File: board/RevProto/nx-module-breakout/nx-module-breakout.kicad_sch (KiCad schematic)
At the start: 8 parts, among them J1 Conn_02x15_Odd_Even, J2 DF40C-60DS-0.4V(51), J3 Conn_02x15_Odd_Even, J4 Conn_02x15_Odd_Even, J5 DF40C-60DS-0.4V(51), J6 SFV22R-2STE1HLF, J7 SFV22R-2STE1HLF, J8 Conn_02x06_Odd_Even

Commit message: nx module breakout work in progress
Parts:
- J6, J7: footprint RP2350_60QFN_minimal:AMPHENOL_SFV22R-2STE1HLF -> CUSTOM:AMPHENOL_SFV22R-2STE1HLF
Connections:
- net DPHY0_CLK+: now also J7.9 (Pin_9); no longer J6.9 (Pin_9)
- net DPHY0_CLK-: now also J7.8 (Pin_8); no longer J6.8 (Pin_8)
- net DPHY0_D0+: now also J7.3 (Pin_3); no longer J6.3 (Pin_3)
- net DPHY0_D0-: now also J7.2 (Pin_2); no longer J6.2 (Pin_2)
- net DPHY0_D1+: now also J7.6 (Pin_6); no longer J6.6 (Pin_6)
- net DPHY0_D1-: now also J7.5 (Pin_5); no longer J6.5 (Pin_5)
- net DPHY0_D2+: now also J7.12 (Pin_12); no longer J6.12 (Pin_12)
- net DPHY0_D2-: now also J7.11 (Pin_11); no longer J6.11 (Pin_11)
- net DPHY0_D3+: now also J7.15 (Pin_15); no longer J6.15 (Pin_15)
- net DPHY0_D3-: now also J7.14 (Pin_14); no longer J6.14 (Pin_14)
- net DPHY1_CLK+: now also J6.14 (Pin_14); no longer J7.14 (Pin_14)
- net DPHY1_CLK-: now also J6.15 (Pin_15); no longer J7.15 (Pin_15)
- net DPHY1_D0+: now also J6.20 (Pin_20); no longer J7.20 (Pin_20)
- net DPHY1_D0-: now also J6.21 (Pin_21); no longer J7.21 (Pin_21)
- net DPHY1_D1+: now also J6.17 (Pin_17); no longer J7.17 (Pin_17)
- net DPHY1_D1-: now also J6.18 (Pin_18); no longer J7.18 (Pin_18)
- net DPHY1_D2+: now also J6.11 (Pin_11); no longer J7.11 (Pin_11)
- net DPHY1_D2-: now also J6.12 (Pin_12); no longer J7.12 (Pin_12)
- net DPHY1_D3+: now also J6.8 (Pin_8); no longer J7.8 (Pin_8)
- net DPHY1_D3-: now also J6.9 (Pin_9); no longer J7.9 (Pin_9)
- net GND: now also J1.1 (Pin_1), J1.11 (Pin_11), J1.12 (Pin_12), J1.2 (Pin_2), J1.21 (Pin_21), J1.22 (Pin_22), J6.22 (Pin_22), J7.1 (Pin_1); no longer J1.10 (Pin_10), J1.19 (Pin_19), J1.20 (Pin_20), J1.29 (Pin_29), J1.30 (Pin_30), J1.9 (Pin_9), J6.1 (Pin_1), J6.MP (MountPin), J7.22 (Pin_22), J7.MP (MountPin)
- net LED_EN0: now also J6.5 (Pin_5); no longer J6.18 (Pin_18)
- net LED_EN1: now also J7.18 (Pin_18); no longer J7.5 (Pin_5)
- net P3V3D: now also J6.1 (Pin_1), J7.22 (Pin_22); no longer J6.22 (Pin_22), J7.1 (Pin_1)
- net PB56N: now also J1.14 (Pin_14); no longer J1.11 (Pin_11)
- net PB56P: now also J1.13 (Pin_13); no longer J1.12 (Pin_12)
- net PB58N: now also J1.7 (Pin_7); no longer J1.6 (Pin_6)
- net PB58P: now also J1.8 (Pin_8); no longer J1.5 (Pin_5)
- net PB60N: now also J1.9 (Pin_9); no longer J1.8 (Pin_8)
- net PB60P: now also J1.10 (Pin_10); no longer J1.7 (Pin_7)
- net PB62N: now also J1.16 (Pin_16); no longer J1.13 (Pin_13)
- net PB62P: now also J1.15 (Pin_15); no longer J1.14 (Pin_14)
- net PB64N: now also J1.17 (Pin_17); no longer J1.16 (Pin_16)
- net PB64P: now also J1.18 (Pin_18); no longer J1.15 (Pin_15)
- net PB66N: now also J1.19 (Pin_19); no longer J1.18 (Pin_18)
- net PB66P: now also J1.20 (Pin_20); no longer J1.17 (Pin_17)
- net PB68N: now also J1.23 (Pin_23); no longer J1.22 (Pin_22)
- net PB68P: now also J1.24 (Pin_24); no longer J1.21 (Pin_21)
- net PB70N: now also J1.26 (Pin_26); no longer J1.23 (Pin_23)
- net PB70P: now also J1.25 (Pin_25); no longer J1.24 (Pin_24)
- net PR11N: now also J1.29 (Pin_29); no longer J1.28 (Pin_28)
- net PR11P: now also J1.30 (Pin_30); no longer J1.27 (Pin_27)
- net PR13N: now also J1.27 (Pin_27); no longer J1.26 (Pin_26)
- net PR13P: now also J1.28 (Pin_28); no longer J1.25 (Pin_25)
- net PR7N: now also J4.27 (Pin_27); no longer J1.3 (Pin_3)
- net PR7P: now also J4.28 (Pin_28); no longer J1.4 (Pin_4)
- net PT67N: now also J4.25 (Pin_25); no longer J1.1 (Pin_1)
- net PT67P: now also J4.26 (Pin_26); no longer J1.2 (Pin_2)
- net PWR_EN0: now also J6.6 (Pin_6); no longer J6.17 (Pin_17)
- net PWR_EN1: now also J7.17 (Pin_17); no longer J7.6 (Pin_6)
- net SCL0: now also J6.3 (Pin_3); no longer J6.20 (Pin_20)
- net SCL1: now also J7.20 (Pin_20); no longer J7.3 (Pin_3)
- net SDA0: now also J6.2 (Pin_2); no longer J6.21 (Pin_21)
- net SDA1: now also J7.21 (Pin_21); no longer J7.2 (Pin_2)
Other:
- moved on the sheet: J1, J2, J3, J4, J5, J6, J7, J8

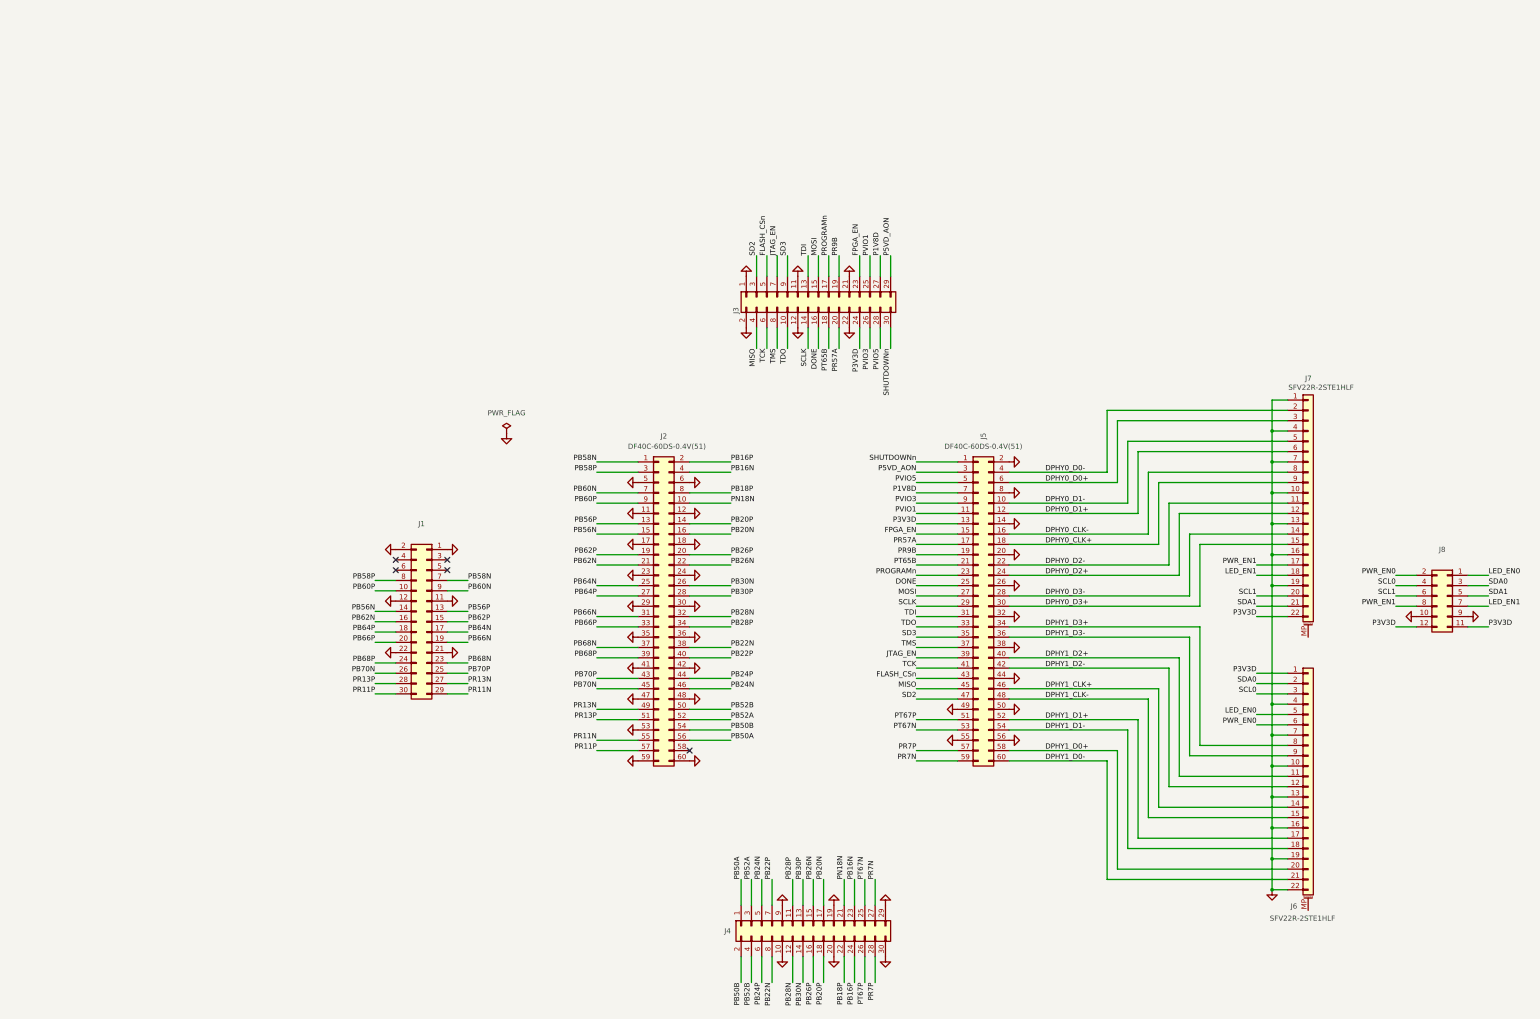
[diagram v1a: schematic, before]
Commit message: Consistent schematic & PCB connector orientation for module, breakout board and pico2-nx.
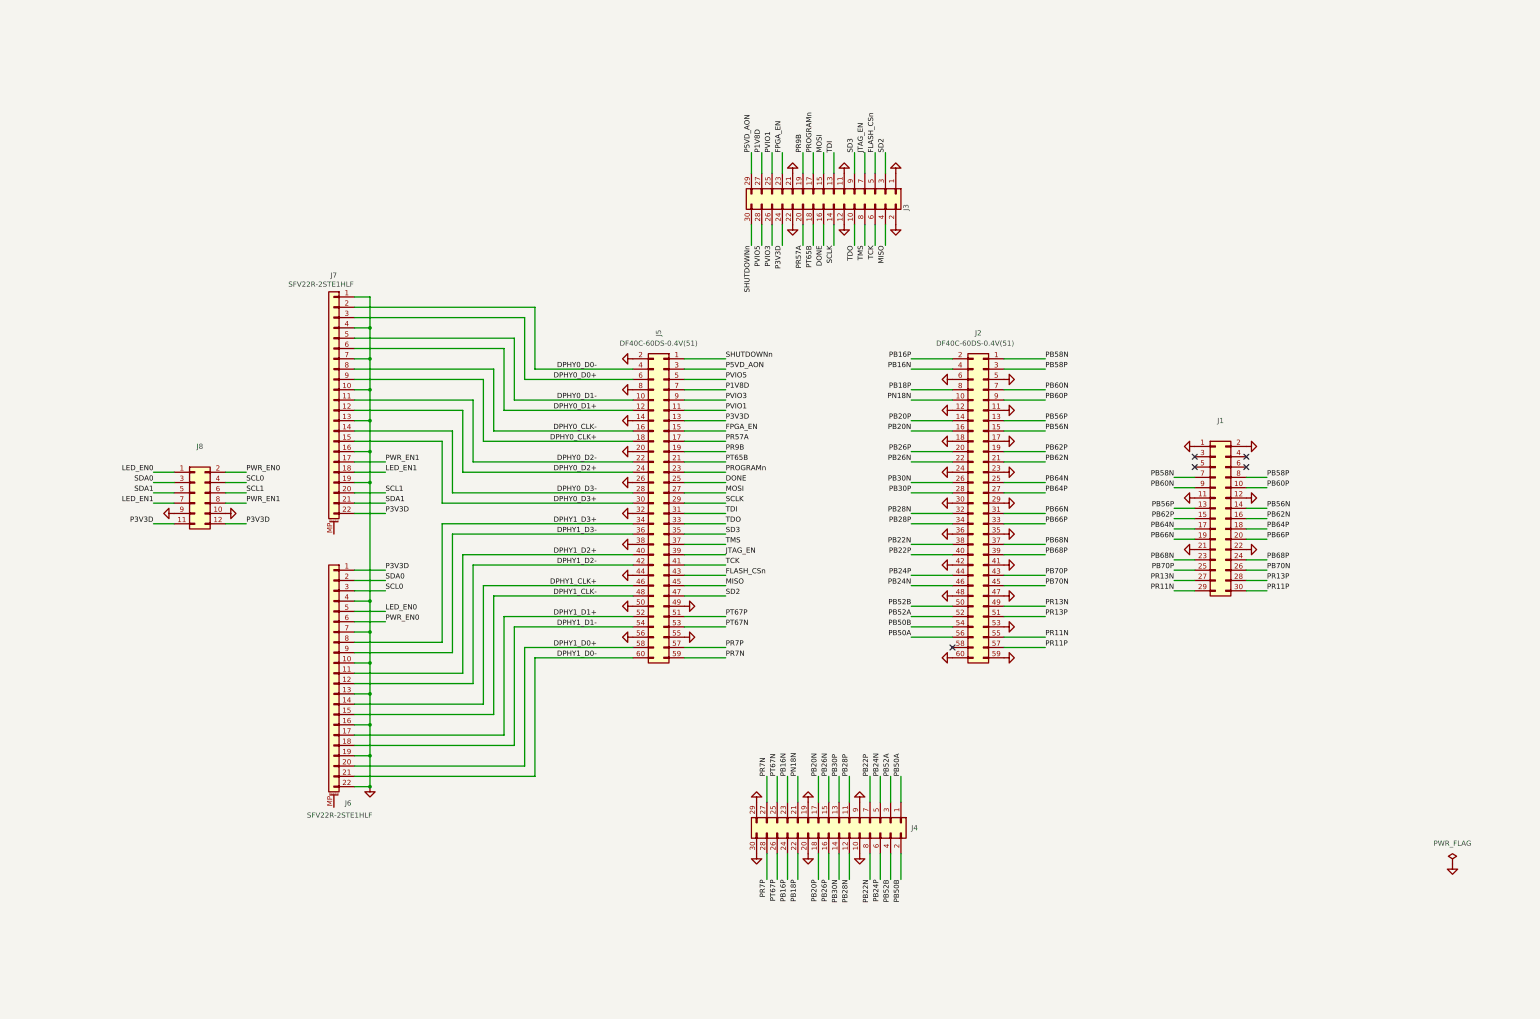
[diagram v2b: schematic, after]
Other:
- moved on the sheet: J1, J2, J3, J4, J5, J6, J7, J8

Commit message: Route breakout
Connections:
- net GND: now also J6.MP (MountPin), J7.MP (MountPin)
- net LED_EN0: now also J8.6 (Pin_6); no longer J8.1 (Pin_1)
- net LED_EN1: now also J8.5 (Pin_5); no longer J8.7 (Pin_7)
- net PB56N: now also J1.13 (Pin_13); no longer J1.14 (Pin_14)
- net PB56P: now also J1.14 (Pin_14); no longer J1.13 (Pin_13)
- net PB58N: now also J1.8 (Pin_8); no longer J1.7 (Pin_7)
- net PB58P: now also J1.7 (Pin_7); no longer J1.8 (Pin_8)
- net PB60N: now also J1.10 (Pin_10); no longer J1.9 (Pin_9)
- net PB60P: now also J1.9 (Pin_9); no longer J1.10 (Pin_10)
- net PB62N: now also J1.15 (Pin_15); no longer J1.16 (Pin_16)
- net PB62P: now also J1.16 (Pin_16); no longer J1.15 (Pin_15)
- net PB64N: now also J1.18 (Pin_18); no longer J1.17 (Pin_17)
- net PB64P: now also J1.17 (Pin_17); no longer J1.18 (Pin_18)
- net PB66N: now also J1.20 (Pin_20); no longer J1.19 (Pin_19)
- net PB66P: now also J1.19 (Pin_19); no longer J1.20 (Pin_20)
- net PB68N: now also J1.24 (Pin_24); no longer J1.23 (Pin_23)
- net PB68P: now also J1.23 (Pin_23); no longer J1.24 (Pin_24)
- net PB70N: now also J1.25 (Pin_25); no longer J1.26 (Pin_26)
- net PB70P: now also J1.26 (Pin_26); no longer J1.25 (Pin_25)
- net PR11N: now also J1.30 (Pin_30); no longer J1.29 (Pin_29)
- net PR11P: now also J1.29 (Pin_29); no longer J1.30 (Pin_30)
- net PR13N: now also J1.28 (Pin_28); no longer J1.27 (Pin_27)
- net PR13P: now also J1.27 (Pin_27); no longer J1.28 (Pin_28)
- net PR7N: now also J4.28 (Pin_28); no longer J4.27 (Pin_27)
- net PR7P: now also J4.27 (Pin_27); no longer J4.28 (Pin_28)
- net PT67N: now also J4.26 (Pin_26); no longer J4.25 (Pin_25)
- net PT67P: now also J4.25 (Pin_25); no longer J4.26 (Pin_26)
- net PWR_EN0: now also J8.8 (Pin_8); no longer J8.2 (Pin_2)
- net PWR_EN1: now also J8.7 (Pin_7); no longer J8.8 (Pin_8)
- net SCL1: now also J8.3 (Pin_3); no longer J8.6 (Pin_6)
- net SDA0: now also J8.2 (Pin_2); no longer J8.3 (Pin_3)
- net SDA1: now also J8.1 (Pin_1); no longer J8.5 (Pin_5)
- net PN18N renamed PB18N

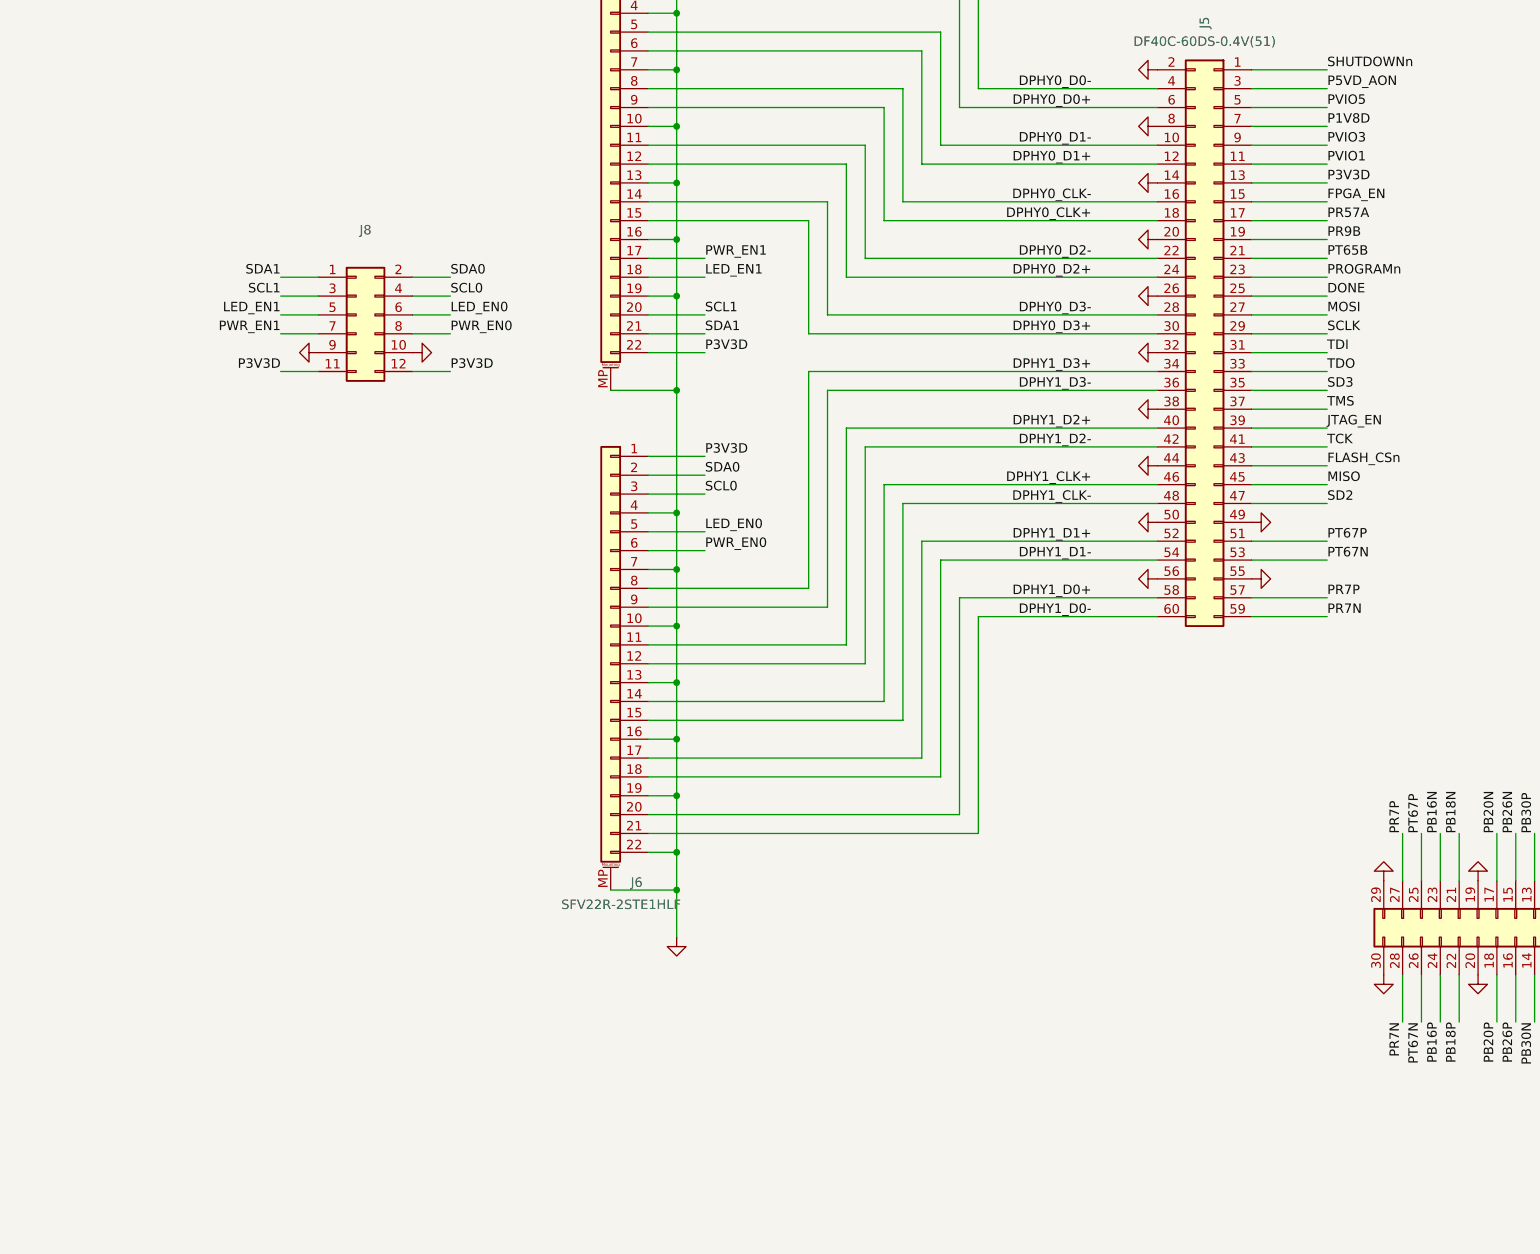
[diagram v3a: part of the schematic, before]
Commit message: Mounting holes. Fiducials. Logos. Beginnings of silk screen
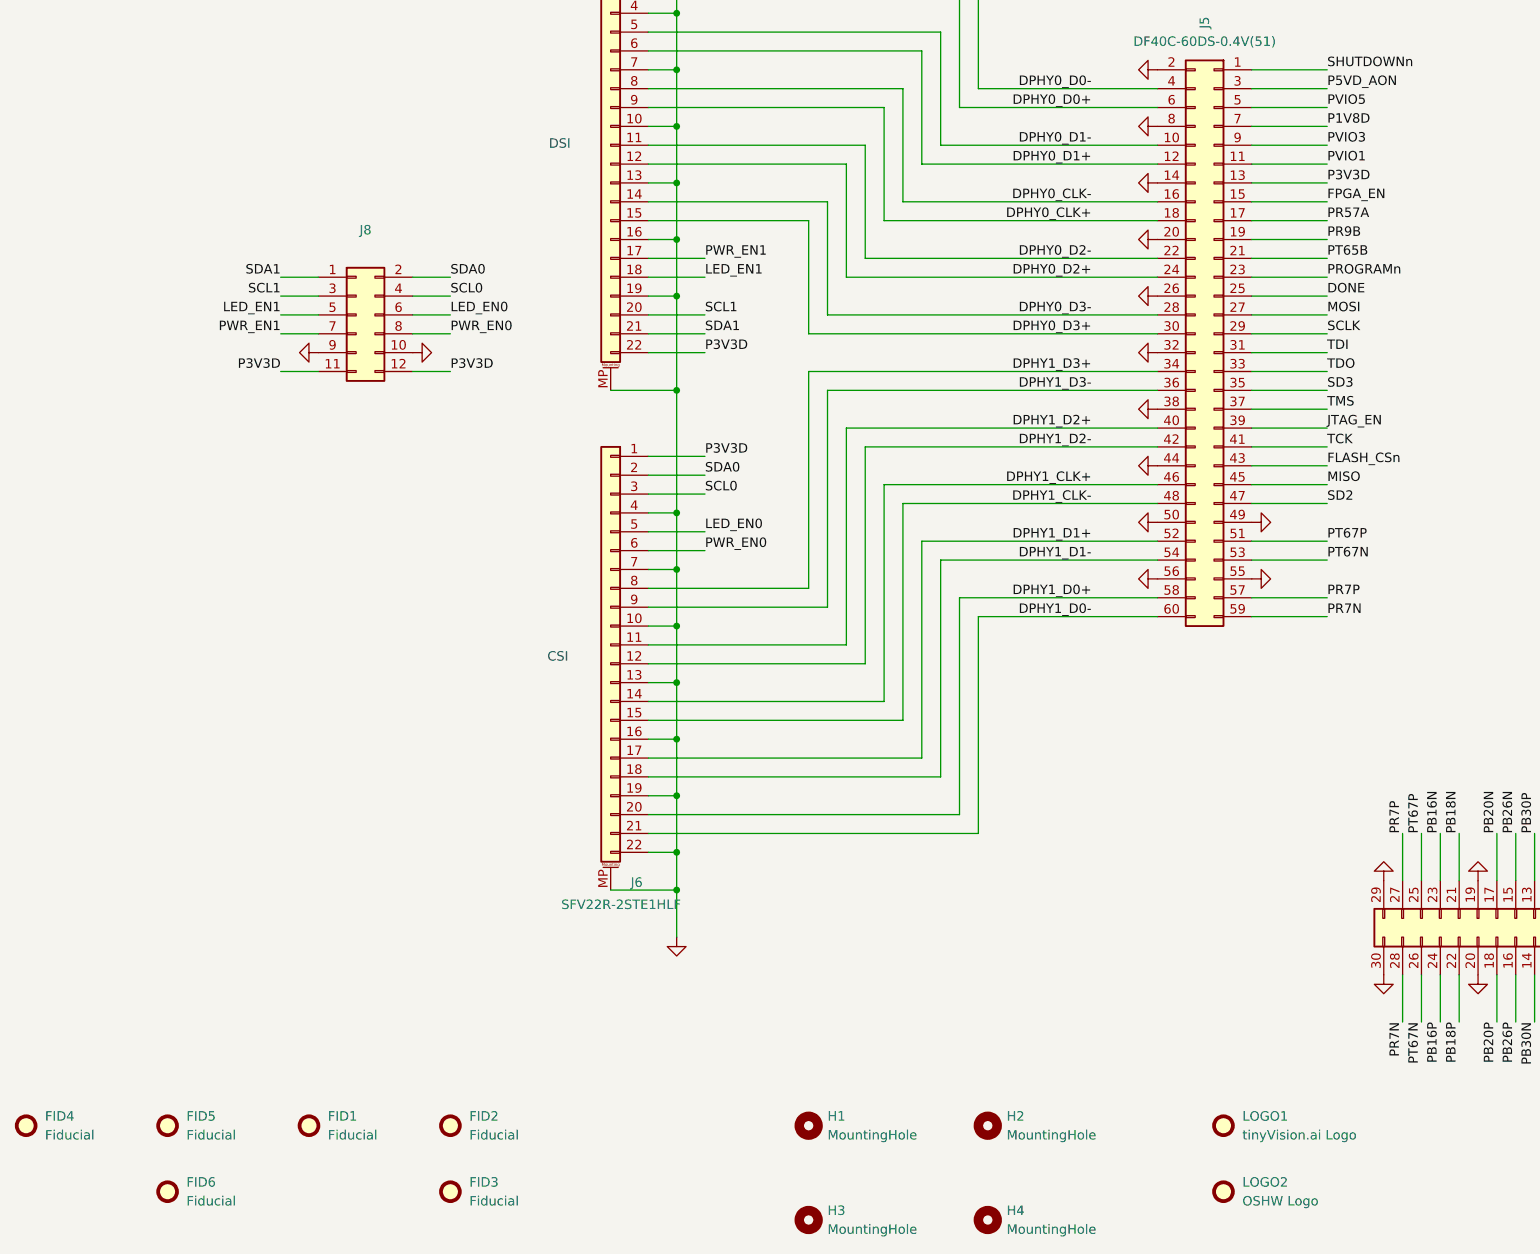
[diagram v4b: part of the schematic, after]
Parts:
- added FID1, FID2, FID3, FID4, FID5, FID6: Fiducial, Fiducial:Fiducial_0.75mm_Mask1.5mm, symbol Mechanical:Fiducial
- added H1, H2, H3, H4: MountingHole, MountingHole:MountingHole_2mm, symbol Mechanical:MountingHole
- added LOGO1: tinyVision.ai Logo, CUSTOM:tinyAI_4_5mm, symbol Mechanical:Fiducial
- added LOGO2: OSHW Logo, CUSTOM:OSHW_Dual_0.1_Scale_2140, symbol Mechanical:Fiducial
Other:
- note added: "CSI"
- note added: "DSI"
- title: (none) -> NX Module Breakout
